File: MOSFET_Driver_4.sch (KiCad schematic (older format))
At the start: 20 parts, among them Q10 TPHR8504PL, Q11 TPHR8504PL, Q12 TPHR8504PL, Q7 TPHR8504PL, Q8 TPHR8504PL, Q9 TPHR8504PL, U1 FD6288Q

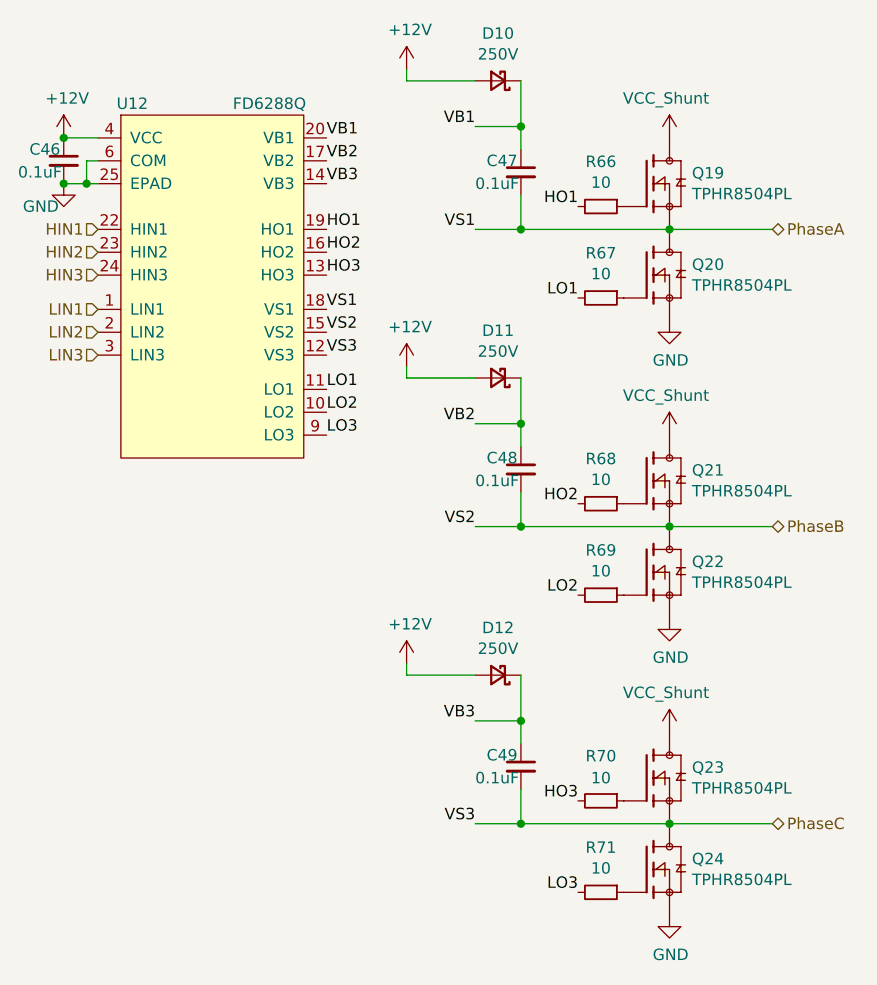
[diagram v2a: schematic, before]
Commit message: Finished all traces and vias
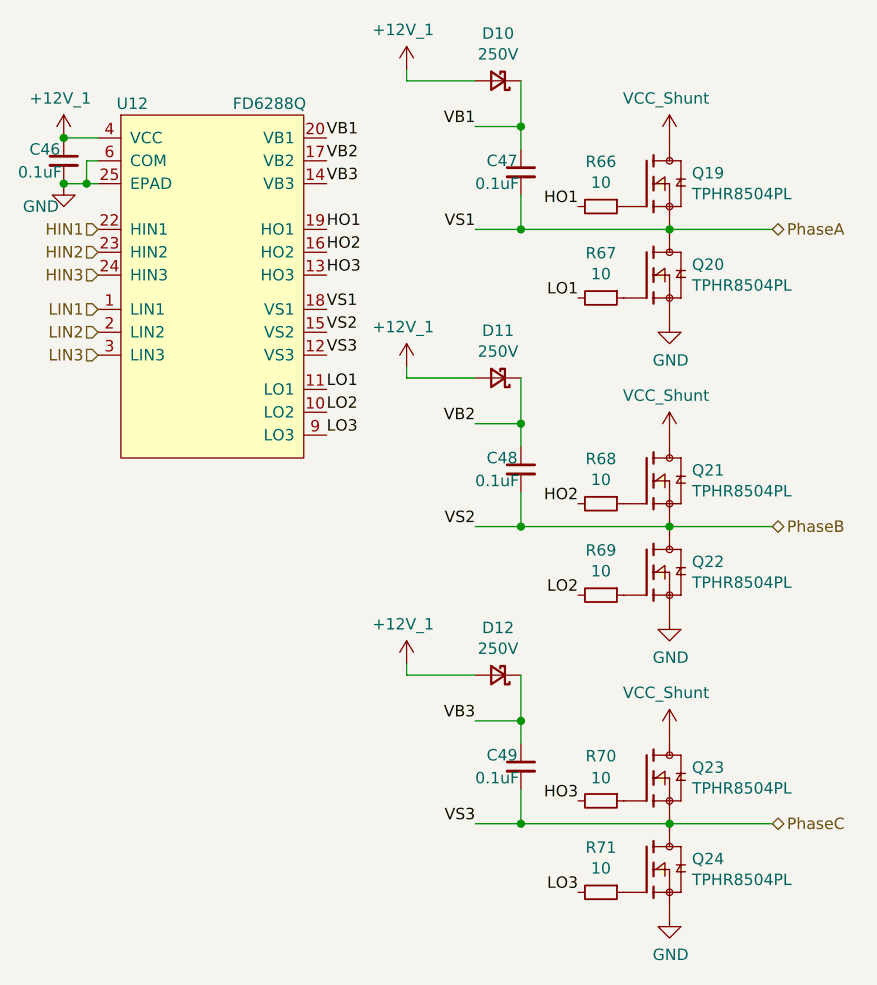
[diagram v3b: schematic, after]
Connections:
- net +12V renamed +12V_1
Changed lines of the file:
@@
 	7500 4850 7500 5000
 Connection ~ 7500 5000
-$Comp
-L power:+12V #PWR02
-U 1 1 60355463
-P 5500 2000
-AR Path="/6035042B/60355463" Ref="#PWR02"  Part="1"
-AR Path="/605793F0/60355463" Ref="#PWR0140"  Part="1"
-AR Path="/6057AB51/60355463" Ref="#PWR?"  Part="1"
-AR Path="/60597CFF/60355463" Ref="#PWR0194"  Part="1"
-AR Path="/60653AB4/60355463" Ref="#PWR?"  Part="1"
-AR Path="/6057505F/60355463" Ref="#PWR0209"  Part="1"
-AR Path="/605A2EC4/60355463" Ref="#PWR0209"  Part="1"
-AR Path="/60551876/60355463" Ref="#PWR0227"  Part="1"
-F 0 "#PWR0227" H 5500 1850 50  0001 C CNN
-F 1 "+12V" H 5515 2173 50  0000 C CNN
-F 2 "" H 5500 2000 50  0001 C CNN
-F 3 "" H 5500 2000 50  0001 C CNN
-	1    5500 2000
-	1    0    0    -1
-$EndComp
-$Comp
-L power:+12V #PWR03
-U 1 1 60663699
-P 7000 3000
-AR Path="/6035042B/60663699" Ref="#PWR03"  Part="1"
-AR Path="/605793F0/60663699" Ref="#PWR0141"  Part="1"
-AR Path="/6057AB51/60663699" Ref="#PWR?"  Part="1"
-AR Path="/60597CFF/60663699" Ref="#PWR0195"  Part="1"
-AR Path="/60653AB4/60663699" Ref="#PWR?"  Part="1"
-AR Path="/6057505F/60663699" Ref="#PWR0210"  Part="1"
-AR Path="/605A2EC4/60663699" Ref="#PWR0210"  Part="1"
-AR Path="/60551876/60663699" Ref="#PWR0228"  Part="1"
-F 0 "#PWR0228" H 7000 2850 50  0001 C CNN
-F 1 "+12V" H 7015 3173 50  0000 C CNN
-F 2 "" H 7000 3000 50  0001 C CNN
-F 3 "" H 7000 3000 50  0001 C CNN
-	1    7000 3000
-	1    0    0    -1
-$EndComp
-$Comp
-L power:+12V #PWR01
-U 1 1 606636A3
-P 7000 1700
-AR Path="/6035042B/606636A3" Ref="#PWR01"  Part="1"
-AR Path="/605793F0/606636A3" Ref="#PWR0142"  Part="1"
-AR Path="/6057AB51/606636A3" Ref="#PWR?"  Part="1"
-AR Path="/60597CFF/606636A3" Ref="#PWR0196"  Part="1"
-AR Path="/60653AB4/606636A3" Ref="#PWR?"  Part="1"
-AR Path="/6057505F/606636A3" Ref="#PWR0211"  Part="1"
-AR Path="/605A2EC4/606636A3" Ref="#PWR0211"  Part="1"
-AR Path="/60551876/606636A3" Ref="#PWR0229"  Part="1"
-F 0 "#PWR0229" H 7000 1550 50  0001 C CNN
-F 1 "+12V" H 7015 1873 50  0000 C CNN
-F 2 "" H 7000 1700 50  0001 C CNN
-F 3 "" H 7000 1700 50  0001 C CNN
-	1    7000 1700
-	1    0    0    -1
-$EndComp
-$Comp
-L power:+12V #PWR04
-U 1 1 606636A4
-P 7000 4300
-AR Path="/6035042B/606636A4" Ref="#PWR04"  Part="1"
-AR Path="/605793F0/606636A4" Ref="#PWR0143"  Part="1"
-AR Path="/6057AB51/606636A4" Ref="#PWR?"  Part="1"
-AR Path="/60597CFF/606636A4" Ref="#PWR0197"  Part="1"
-AR Path="/60653AB4/606636A4" Ref="#PWR?"  Part="1"
-AR Path="/6057505F/606636A4" Ref="#PWR0212"  Part="1"
-AR Path="/605A2EC4/606636A4" Ref="#PWR0212"  Part="1"
-AR Path="/60551876/606636A4" Ref="#PWR0230"  Part="1"
-F 0 "#PWR0230" H 7000 4150 50  0001 C CNN
-F 1 "+12V" H 7015 4473 50  0000 C CNN
-F 2 "" H 7000 4300 50  0001 C CNN
-F 3 "" H 7000 4300 50  0001 C CNN
-	1    7000 4300
-	1    0    0    -1
-$EndComp
 $Bitmap
 Pos 4150 2500
@@
 Wire Wire Line
 	5500 2000 5650 2000
-Connection ~ 5500 2000
 Wire Wire Line
 	5650 2200 5600 2200
@@
 	1    0    0    -1
 $EndComp
+$Comp
+L power:+12V_1 #PWR0199
+U 1 1 606FA00F
+P 5500 2000
+F 0 "#PWR0199" H 5500 1900 50  0001 C CNN
+F 1 "+12V_1" H 5485 2173 50  0000 C CNN
+F 2 "" H 5500 2000 50  0001 C CNN
+F 3 "" H 5500 2000 50  0001 C CNN
+	1    5500 2000
+	1    0    0    -1
+$EndComp
+Connection ~ 5500 2000
+$Comp
+L power:+12V_1 #PWR0227
+U 1 1 606FA754
+P 7000 1700
+F 0 "#PWR0227" H 7000 1600 50  0001 C CNN
+F 1 "+12V_1" H 6985 1873 50  0000 C CNN
+F 2 "" H 7000 1700 50  0001 C CNN
+F 3 "" H 7000 1700 50  0001 C CNN
+	1    7000 1700
+	1    0    0    -1
+$EndComp
+$Comp
+L power:+12V_1 #PWR0228
+U 1 1 606FADC0
+P 7000 3000
+F 0 "#PWR0228" H 7000 2900 50  0001 C CNN
+F 1 "+12V_1" H 6985 3173 50  0000 C CNN
+F 2 "" H 7000 3000 50  0001 C CNN
+F 3 "" H 7000 3000 50  0001 C CNN
+	1    7000 3000
+	1    0    0    -1
+$EndComp
+$Comp
+L power:+12V_1 #PWR0229
+U 1 1 606FB2C7
+P 7000 4300
+F 0 "#PWR0229" H 7000 4200 50  0001 C CNN
+F 1 "+12V_1" H 6985 4473 50  0000 C CNN
+F 2 "" H 7000 4300 50  0001 C CNN
+F 3 "" H 7000 4300 50  0001 C CNN
+	1    7000 4300
+	1    0    0    -1
+$EndComp
